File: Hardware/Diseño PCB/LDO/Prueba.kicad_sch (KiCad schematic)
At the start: 55 parts, among them Q1 2N3904, Q10 BC557, Q11 BC547, Q12 BC557, Q13 2N3906, Q14 2N3904, Q15 2N3906, Q16 2N3904, Q17 2N3906, Q18 2N3904, Q19 2N3904, Q2 2N3904, Q3 2N3904, Q4 2N3906, Q5 2N3906, Q6 2N3904, Q7 2N3904, Q8 IRF4905, Q9 BC547, U1 TL431LP, U4 LM324

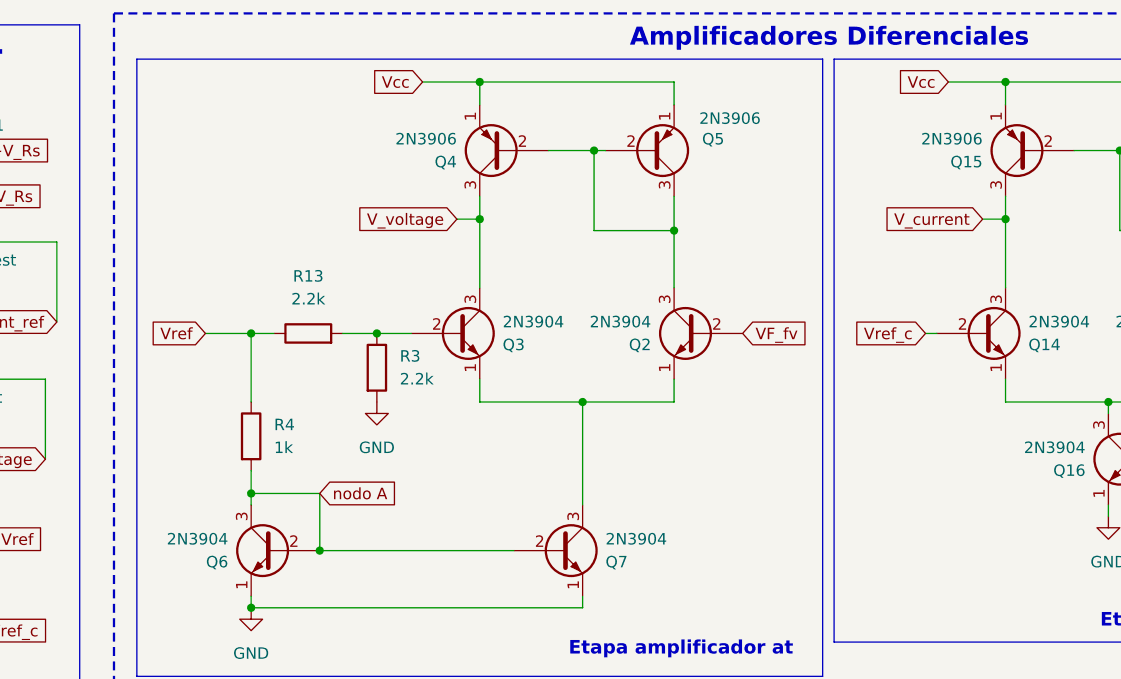
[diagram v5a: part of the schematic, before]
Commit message: Diseño PCB: Informe, orificos de sujeció, C de compensacion
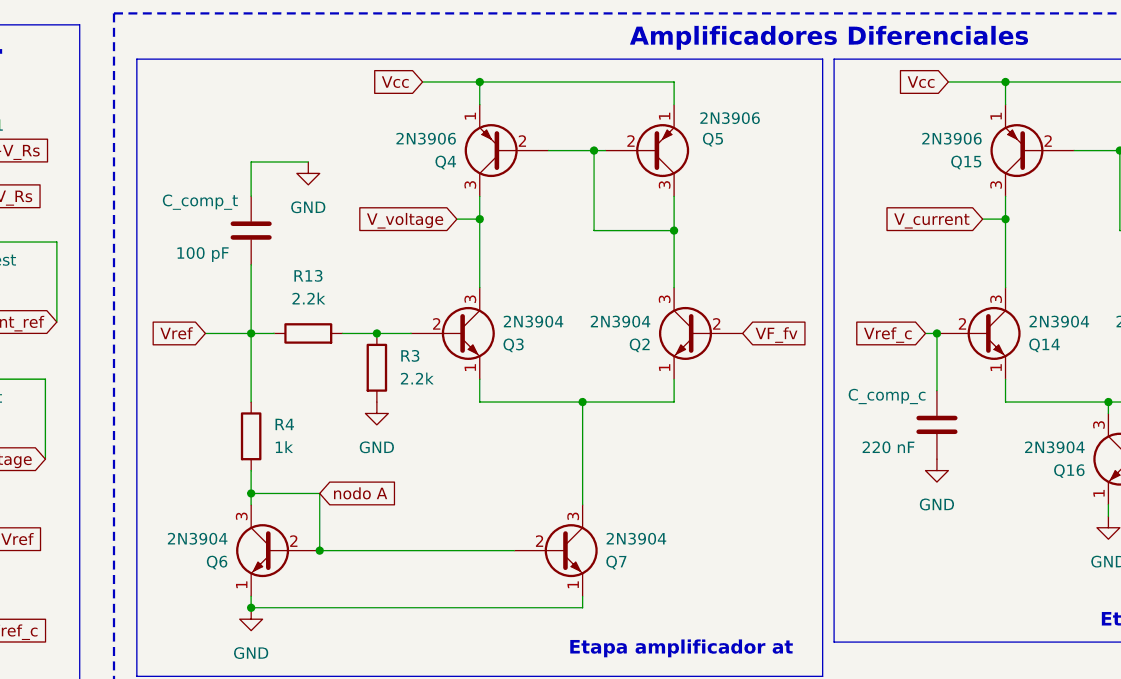
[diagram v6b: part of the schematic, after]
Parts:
- added C_comp_c: 220 nF, symbol Device:C
- added C_comp_t: 100 pF, symbol Device:C
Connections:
- net GND: now also C_comp_c.2, C_comp_t.1
- net Vref: now also C_comp_t.2
- net Vref_c: now also C_comp_c.1

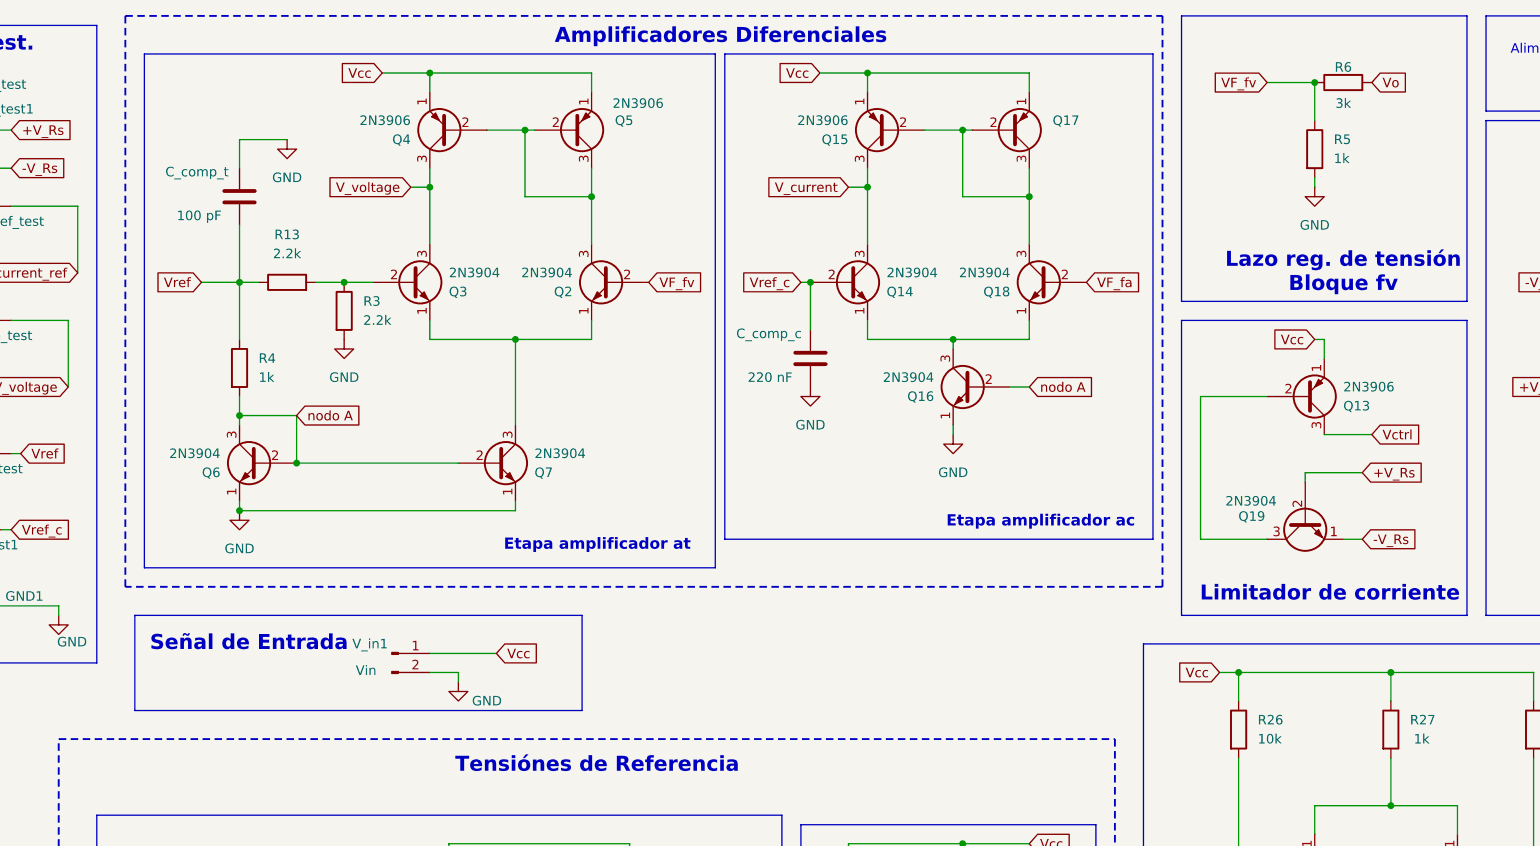
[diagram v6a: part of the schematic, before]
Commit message: Diseño PCB: Transistores BC557/BC547 en esquematico y pcb
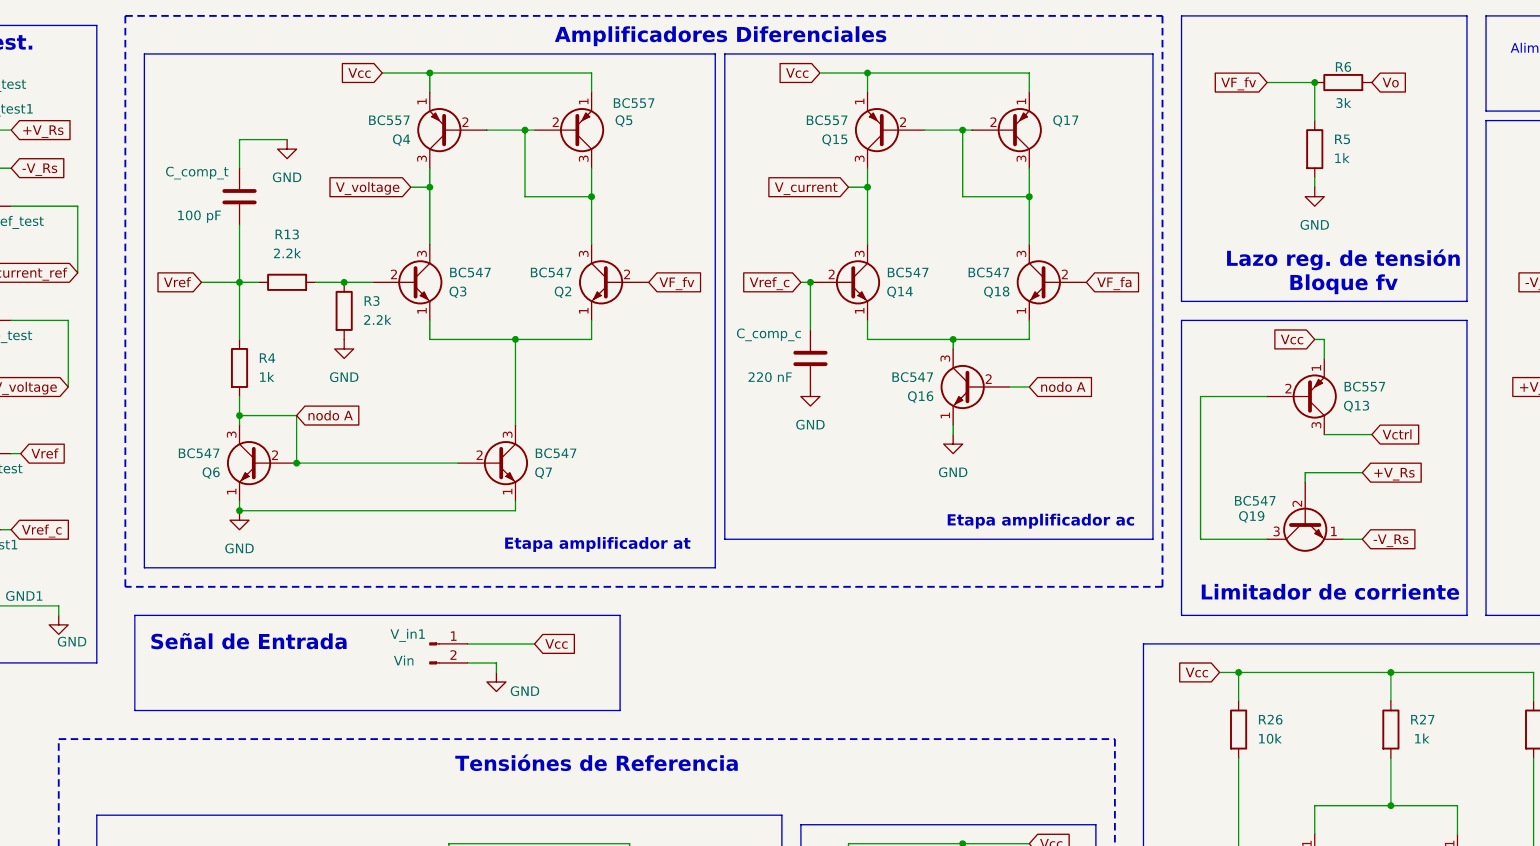
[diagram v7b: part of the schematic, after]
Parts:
- Q13, Q15, Q17, Q4, Q5: value 2N3906 -> BC557
- Q14, Q16, Q18, Q19, Q2, Q3, Q6, Q7: value 2N3904 -> BC547
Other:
- moved on the sheet: V_in1
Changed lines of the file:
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@@
 	(rectangle
 		(start 43.18 93.98)
-		(end 102.87 106.68)
+		(end 107.95 106.68)
 		(stroke
 			(width 0)
@@
 	(wire
 		(pts
-			(xy 86.36 102.87) (xy 86.36 101.6)
+			(xy 91.44 101.6) (xy 91.44 100.33)
 		)
 		(stroke
@@
 	(wire
 		(pts
-			(xy 82.55 99.06) (xy 91.44 99.06)
+			(xy 87.63 97.79) (xy 96.52 97.79)
 		)
 		(stroke
@@
 	(wire
 		(pts
-			(xy 86.36 101.6) (xy 82.55 101.6)
+			(xy 91.44 100.33) (xy 87.63 100.33)
 		)
 		(stroke
@@
 	(global_label "Vcc"
 		(shape input)
-		(at 91.44 99.06 0)
+		(at 96.52 97.79 0)
 		(fields_autoplaced yes)
 		(effects
@@
 		)
 		(property "Intersheetrefs" "${INTERSHEET_REFS}"
-			(at 97.691 99.06 0)
+			(at 102.771 97.79 0)
 			(hide yes)
 			(show_name no)
@@
 			)
 		)
-		(property "Value" "2N3904"
+		(property "Value" "BC547"
 			(at 96.52 72.3901 0)
 			(show_name no)
@@
 			)
 		)
-		(property "Value" "2N3904"
+		(property "Value" "BC547"
 			(at 101.6 48.2601 0)
 			(show_name no)
@@
 			)
 		)
-		(property "Value" "2N3906"
+		(property "Value" "BC557"
 			(at 106.934 25.654 0)
 			(show_name no)
@@
 	(symbol
 		(lib_id "power:GND")
-		(at 86.36 102.87 0)
+		(at 91.44 101.6 0)
 		(unit 1)
 		(body_style 1)
@@
 		(dnp no)
 		(property "Reference" "#PWR023"
-			(at 86.36 109.22 0)
+			(at 91.44 107.95 0)
 			(hide yes)
 			(show_name no)
@@
 		)
 		(property "Value" "GND"
-			(at 90.17 105.41 0)
+			(at 95.25 104.14 0)
 			(show_name no)
 			(do_not_autoplace no)
@@
 		)
 		(property "Footprint" ""
-			(at 86.36 102.87 0)
+			(at 91.44 101.6 0)
 			(hide yes)
 			(show_name no)
@@
 		)
 		(property "Datasheet" ""
-			(at 86.36 102.87 0)
+			(at 91.44 101.6 0)
 			(hide yes)
 			(show_name no)
@@
 		)
 		(property "Description" "Power symbol creates a global label with name \"GND\" , ground"
-			(at 86.36 102.87 0)
+			(at 91.44 101.6 0)
 			(hide yes)
 			(show_name no)
@@
 			)
 		)
-		(property "Value" "2N3906"
+		(property "Value" "BC557"
 			(at 165.354 25.654 0)
 			(hide yes)
@@
 			)
 		)
-		(property "Value" "2N3906"
+		(property "Value" "BC557"
 			(at 204.47 63.5001 0)
 			(show_name no)
@@
 			)
 		)
-		(property "Value" "2N3904"
+		(property "Value" "BC547"
 			(at 160.02 48.2601 0)
 			(show_name no)
@@
 			)
 		)
-		(property "Value" "2N3904"
+		(property "Value" "BC547"
 			(at 149.86 62.2301 0)
 			(show_name no)
@@
 			)
 		)
-		(property "Value" "2N3904"
+		(property "Value" "BC547"
 			(at 85.09 48.2601 0)
 			(show_name no)
@@
 	(symbol
 		(lib_id "Connector:Conn_01x02_Pin")
-		(at 77.47 99.06 0)
+		(at 82.55 97.79 0)
 		(unit 1)
 		(body_style 1)
@@
 		(dnp no)
 		(property "Reference" "V_in1"
-			(at 76.962 97.79 0)
+			(at 82.042 96.52 0)
 			(show_name no)
 			(do_not_autoplace no)
@@
 		)
 		(property "Value" "Vin"
-			(at 75.438 101.346 0)
+			(at 80.518 100.076 0)
 			(show_name no)
 			(do_not_autoplace no)
@@
 		)
 		(property "Footprint" "Connector_PinHeader_2.00mm:PinHeader_1x02_P2.00mm_Vertical"
-			(at 77.47 99.06 0)
+			(at 82.55 97.79 0)
 			(hide yes)
 			(show_name no)
@@
 		)
 		(property "Datasheet" ""
-			(at 77.47 99.06 0)
+			(at 82.55 97.79 0)
 			(hide yes)
 			(show_name no)
@@
 		)
 		(property "Description" "Generic connector, single row, 01x02, script generated"
-			(at 77.47 99.06 0)
+			(at 82.55 97.79 0)
 			(hide yes)
 			(show_name no)
@@
 			)
 		)
-		(property "Value" "2N3904"
+		(property "Value" "BC547"
 			(at 195.58 78.74 90)
 			(show_name no)
@@
 			)
 		)
-		(property "Value" "2N3906"
+		(property "Value" "BC557"
 			(at 80.01 27.9401 0)
 			(show_name no)
@@
 			)
 		)
-		(property "Value" "2N3904"
+		(property "Value" "BC547"
 			(at 143.51 48.2601 0)
 			(show_name no)
@@
 			)
 		)
-		(property "Value" "2N3904"
+		(property "Value" "BC547"
 			(at 54.61 72.3901 0)
 			(show_name no)
@@
 			)
 		)
-		(property "Value" "2N3906"
+		(property "Value" "BC557"
 			(at 138.43 27.9401 0)
 			(show_name no)

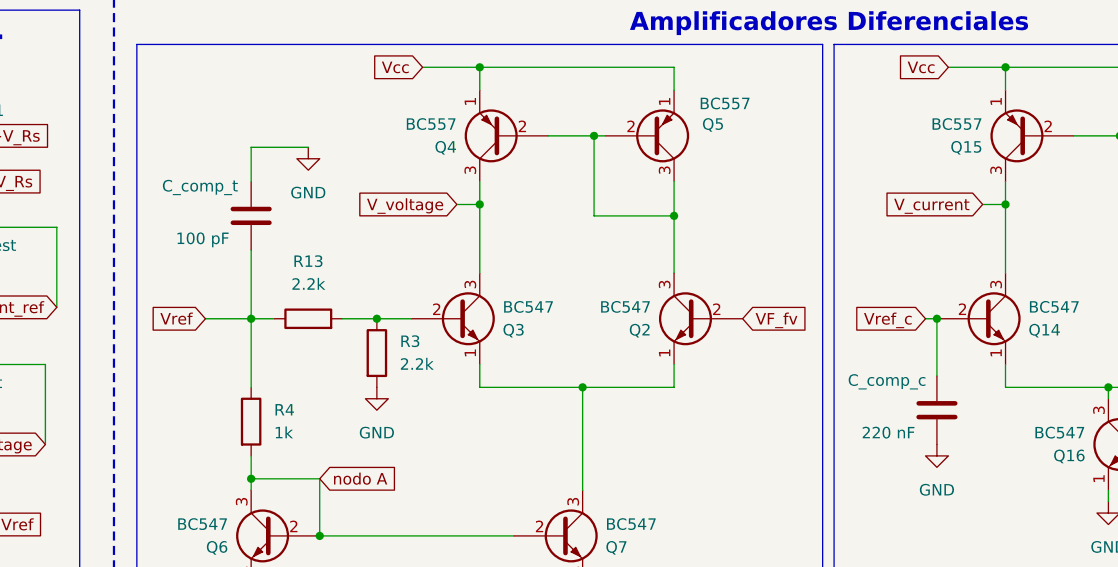
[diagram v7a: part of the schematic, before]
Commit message: Diseño PCB: Pistas y C compensacion en Pcb
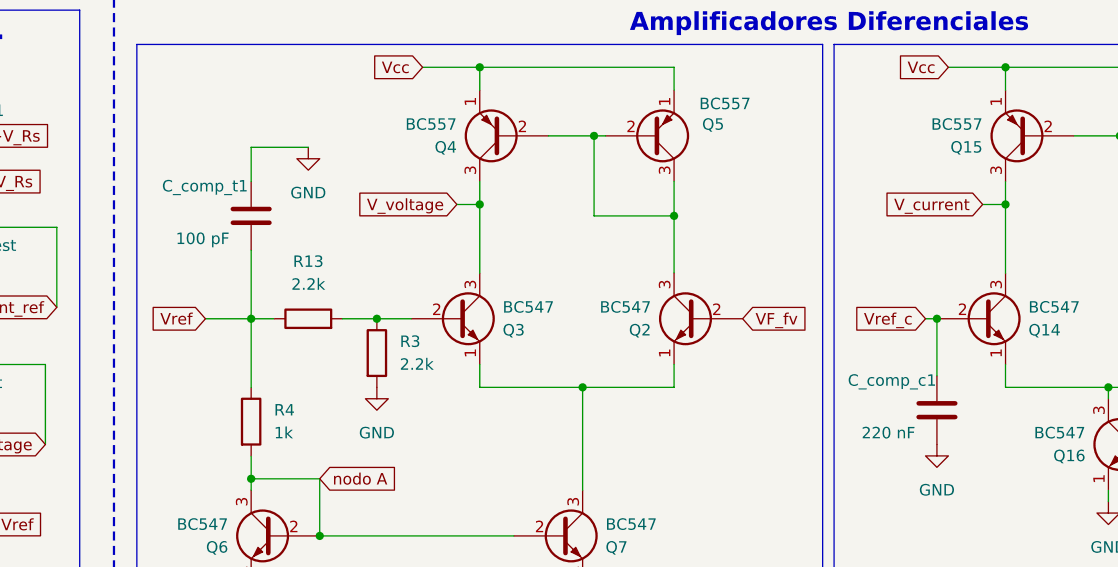
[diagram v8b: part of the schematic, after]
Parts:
- C_comp_c1: renamed from C_comp_c; footprint (none) -> Capacitor_THT:C_Disc_D3.8mm_W2.6mm_P2.50mm
- C_comp_t1: renamed from C_comp_t; footprint (none) -> Capacitor_THT:C_Disc_D3.8mm_W2.6mm_P2.50mm
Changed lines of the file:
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@@
 		(in_pos_files yes)
 		(dnp no)
-		(property "Reference" "C_comp_t"
+		(property "Reference" "C_comp_t1"
 			(at 47.244 34.798 0)
 			(show_name no)
@@
 			)
 		)
-		(property "Footprint" ""
+		(property "Footprint" "Capacitor_THT:C_Disc_D3.8mm_W2.6mm_P2.50mm"
 			(at 58.1152 41.91 0)
 			(hide yes)
@@
 			(project "Prueba"
 				(path "/70bda0a3-0c17-43ce-af47-54d014630cec"
-					(reference "C_comp_t")
+					(reference "C_comp_t1")
 					(unit 1)
 				)
@@
 		(in_pos_files yes)
 		(dnp no)
-		(property "Reference" "C_comp_c"
+		(property "Reference" "C_comp_c1"
 			(at 123.444 56.388 0)
 			(show_name no)
@@
 			)
 		)
-		(property "Footprint" ""
+		(property "Footprint" "Capacitor_THT:C_Disc_D3.8mm_W2.6mm_P2.50mm"
 			(at 134.3152 63.5 0)
 			(hide yes)
@@
 			(project "Prueba"
 				(path "/70bda0a3-0c17-43ce-af47-54d014630cec"
-					(reference "C_comp_c")
+					(reference "C_comp_c1")
 					(unit 1)
 				)
